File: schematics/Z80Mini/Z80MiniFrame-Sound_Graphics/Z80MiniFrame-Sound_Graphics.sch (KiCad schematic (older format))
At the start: 2 parts, among them J1 Conn_02x20_Odd_Even

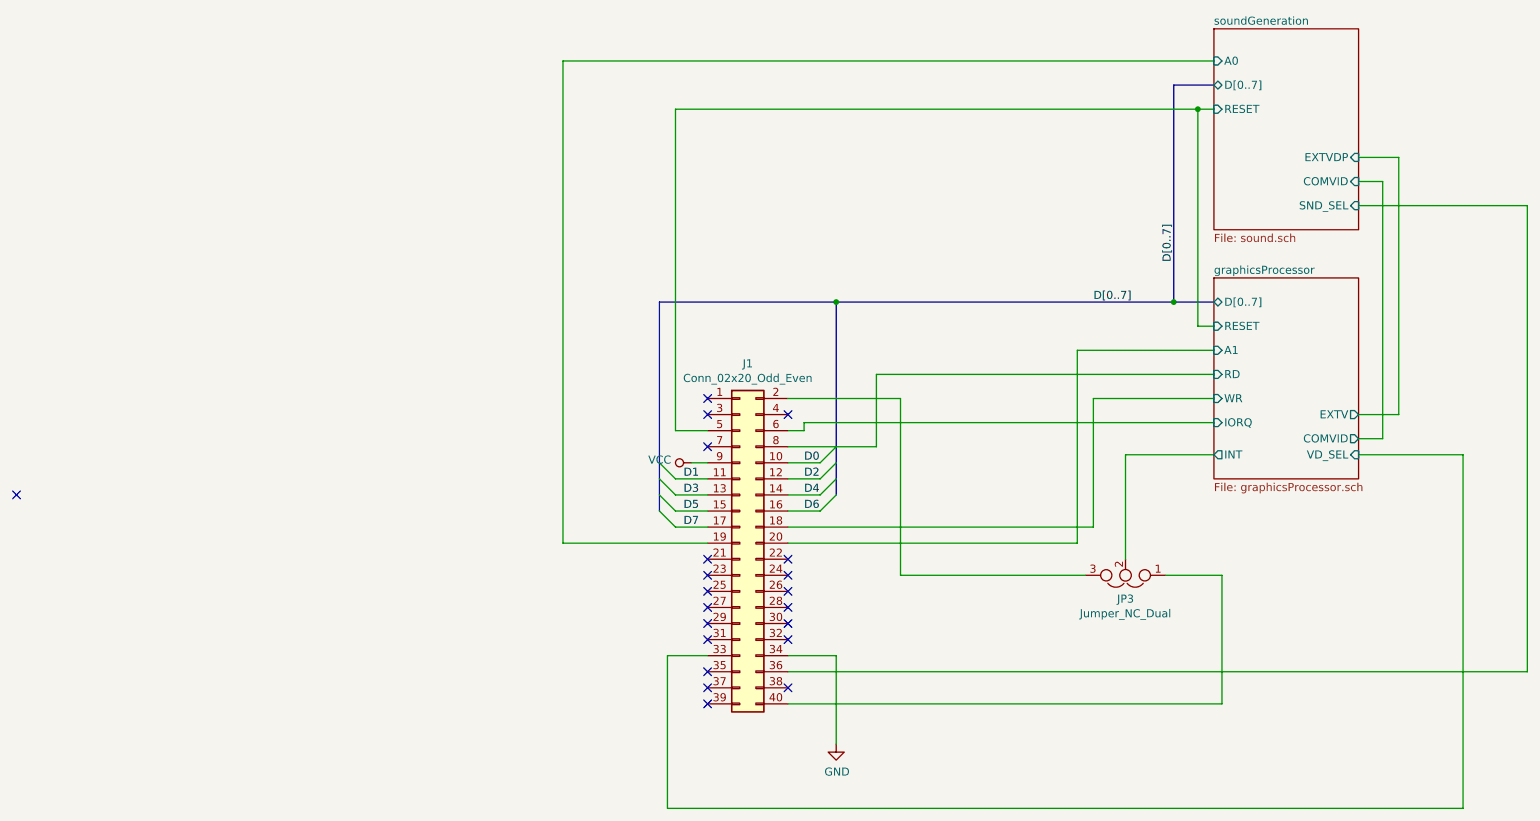
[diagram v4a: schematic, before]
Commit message: Testing C routines for VDP and keyboard. Generated backplane gerber files
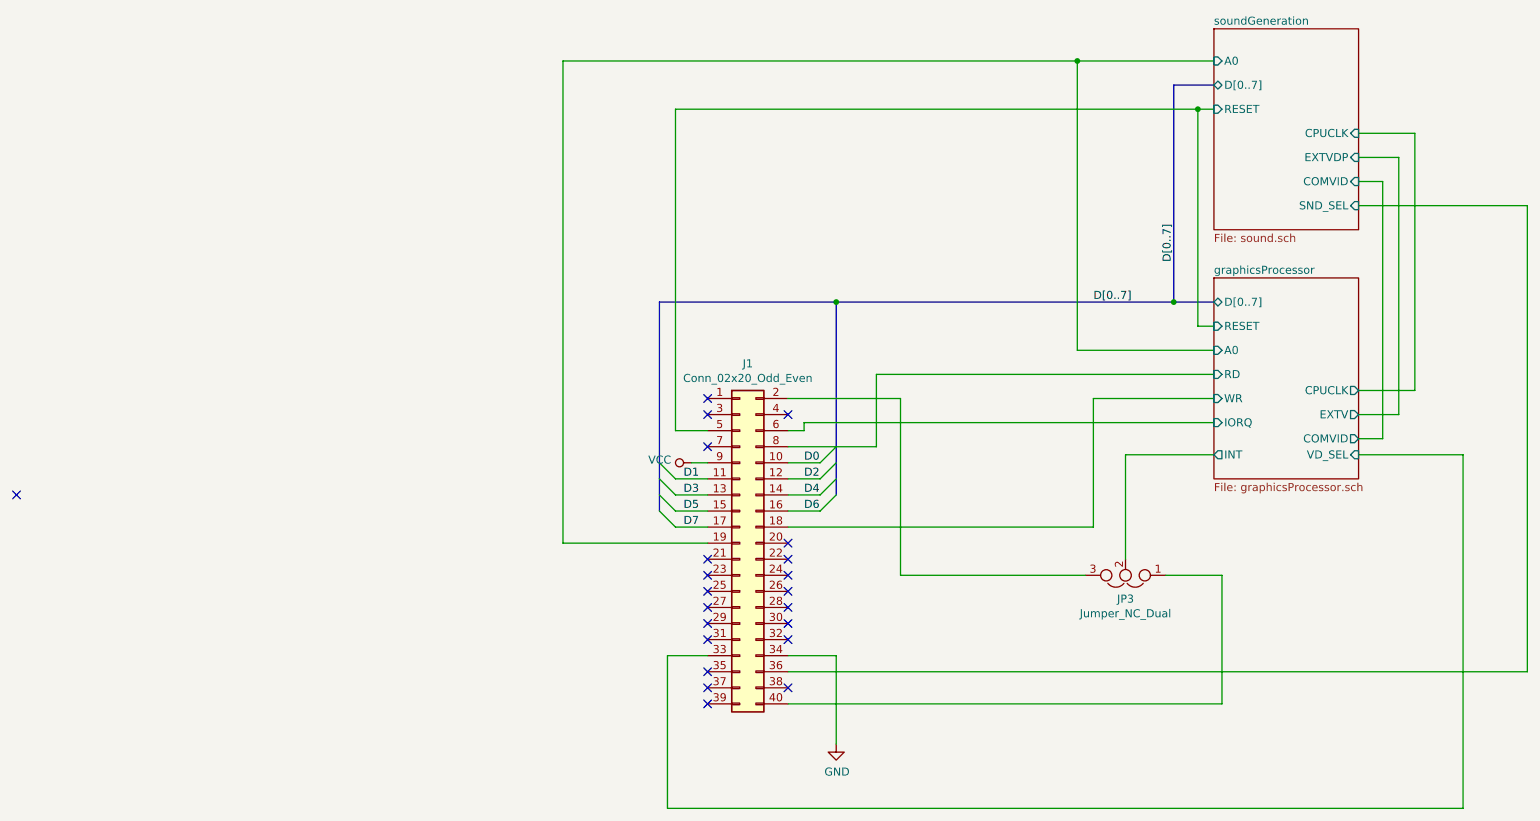
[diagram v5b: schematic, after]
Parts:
- JP3: footprint Connector_PinHeader_2.00mm:PinHeader_1x03_P2.00mm_Vertical -> Connector_PinHeader_2.54mm:PinHeader_1x03_P2.54mm_Vertical
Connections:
- net graphicsProcessor/A1: no longer names the net of J1.20 (Pin_20)
- net soundGeneration/A0 renamed graphicsProcessor/A0
- no-connect marks 21 -> 22
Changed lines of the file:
@@
 F2 "D[0..7]" B L 5050 3800 50
 F3 "RESET" I L 5050 3950 50
-F4 "A1" I L 5050 4100 50
+F4 "A0" I L 5050 4100 50
 F5 "RD" I L 5050 4250 50
 F6 "WR" I L 5050 4400 50
@@
 F10 "EXTV" O R 5950 4500 50
 F11 "COMVID" O R 5950 4650 50
+F12 "CPUCLK" O R 5950 4350 50
 $EndSheet
 $Sheet
@@
 F6 "COMVID" I R 5950 3050 50
 F7 "EXTVDP" I R 5950 2900 50
+F8 "CPUCLK" I R 5950 2750 50
 $EndSheet
 Wire Wire Line
-	1000 2300 5050 2300
+	1000 2300 4200 2300
 Wire Wire Line
 	1000 5300 1900 5300
@@
 Wire Wire Line
 	4950 2600 1700 2600
-Wire Wire Line
-	2400 5300 4200 5300
-Wire Wire Line
-	4200 5300 4200 4100
 Wire Wire Line
 	5050 4250 2950 4250
@@
 F 0 "JP3" H 4500 5647 50  0000 C CNN
 F 1 "Jumper_NC_Dual" H 4500 5738 50  0000 C CNN
-F 2 "Connector_PinHeader_2.00mm:PinHeader_1x03_P2.00mm_Vertical" H 4500 5500 50  0001 C CNN
+F 2 "Connector_PinHeader_2.54mm:PinHeader_1x03_P2.54mm_Vertical" H 4500 5500 50  0001 C CNN
 F 3 "~" H 4500 5500 50  0001 C CNN
 	1    4500 5500
@@
 Wire Wire Line
 	5100 6300 2400 6300
+NoConn ~ 2400 5300
+Connection ~ 4200 2300
+Wire Wire Line
+	4200 2300 5050 2300
+Wire Wire Line
+	4200 2300 4200 4100
+Wire Wire Line
+	5950 4350 6300 4350
+Wire Wire Line
+	6300 4350 6300 2750
+Wire Wire Line
+	6300 2750 5950 2750
 Wire Wire Line
 	2400 4700 2950 4700

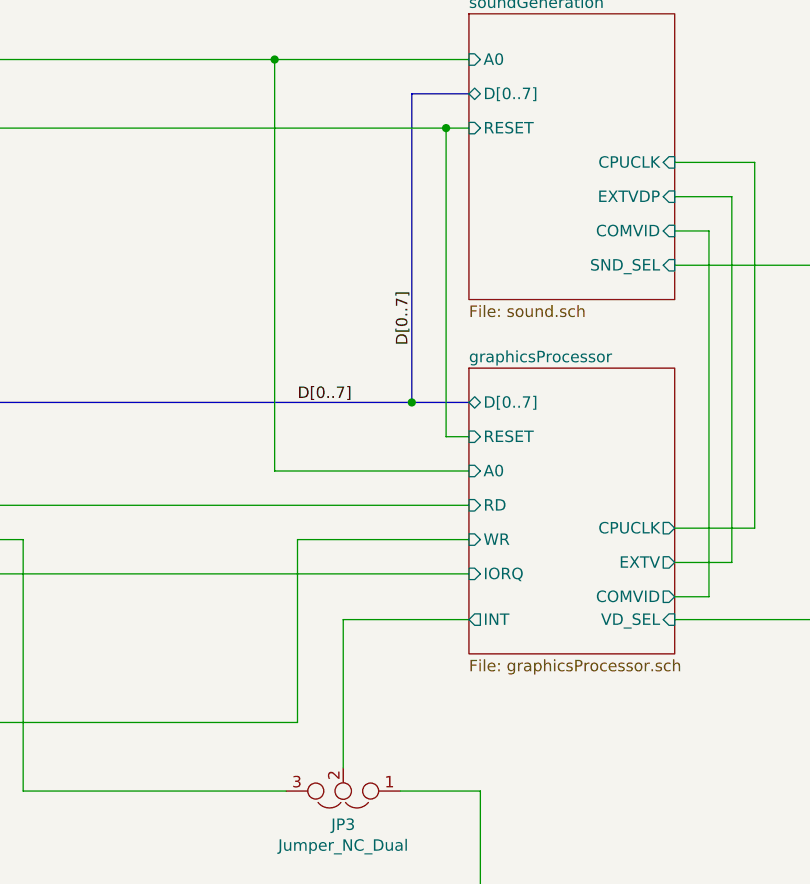
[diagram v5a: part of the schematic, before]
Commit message: Latest code changes and modified Makefile to support burn to EPROM Emulator
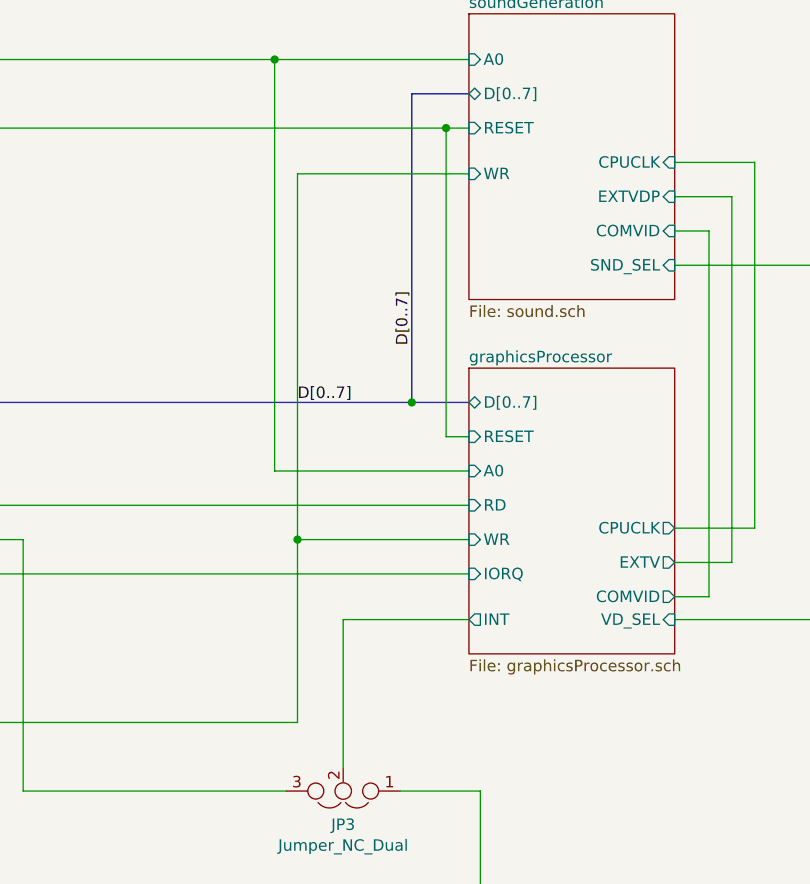
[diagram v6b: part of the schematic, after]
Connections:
- net graphicsProcessor/WR is gone; now on net D[0..7]: J1.18 (Pin_18)
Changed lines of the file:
@@
 EESchema Schematic File Version 4
-LIBS:Z80MiniFrame-Sound_Graphics-cache
 EELAYER 30 0
 EELAYER END
@@
 F7 "EXTVDP" I R 5950 2900 50
 F8 "CPUCLK" I R 5950 2750 50
+F9 "WR" I L 5050 2800 50
 $EndSheet
 Wire Wire Line
@@
 NoConn ~ 1900 6300
 Wire Wire Line
-	4300 5200 4300 4400
-Wire Wire Line
 	2400 5200 4300 5200
 Wire Wire Line
@@
 	6300 2750 5950 2750
 Wire Wire Line
+	4300 2800 5050 2800
+Wire Wire Line
+	4300 2800 4300 4400
+Wire Wire Line
 	2400 4700 2950 4700
 Wire Bus Line
@@
 Wire Bus Line
 	2700 3800 2700 5000
+Connection ~ 4300 4400
+Wire Wire Line
+	4300 4400 4300 5200
 $EndSCHEMATC

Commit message: Added new schematics for all-in-one microcomputer board
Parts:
- JP3: symbol Device:Jumper_NC_Dual -> Z80MiniFrame-Sound_Graphics-rescue:Jumper_NC_Dual-Device
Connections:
- wire segments 59 -> 60
